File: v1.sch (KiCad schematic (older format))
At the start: 43 parts, among them J1 Conn_01x04, J101 K1X06, J102 FTDI, J103 ISP, J2 Conn_01x04, J3 Conn_01x04, J4 Conn_01x04, J5 Conn_01x04, Q1 AO3400A, SW101 SW_Push, U1 ATmega328P-AU, U3 PST61C24, U4 DS18B20, Y1 8MHz

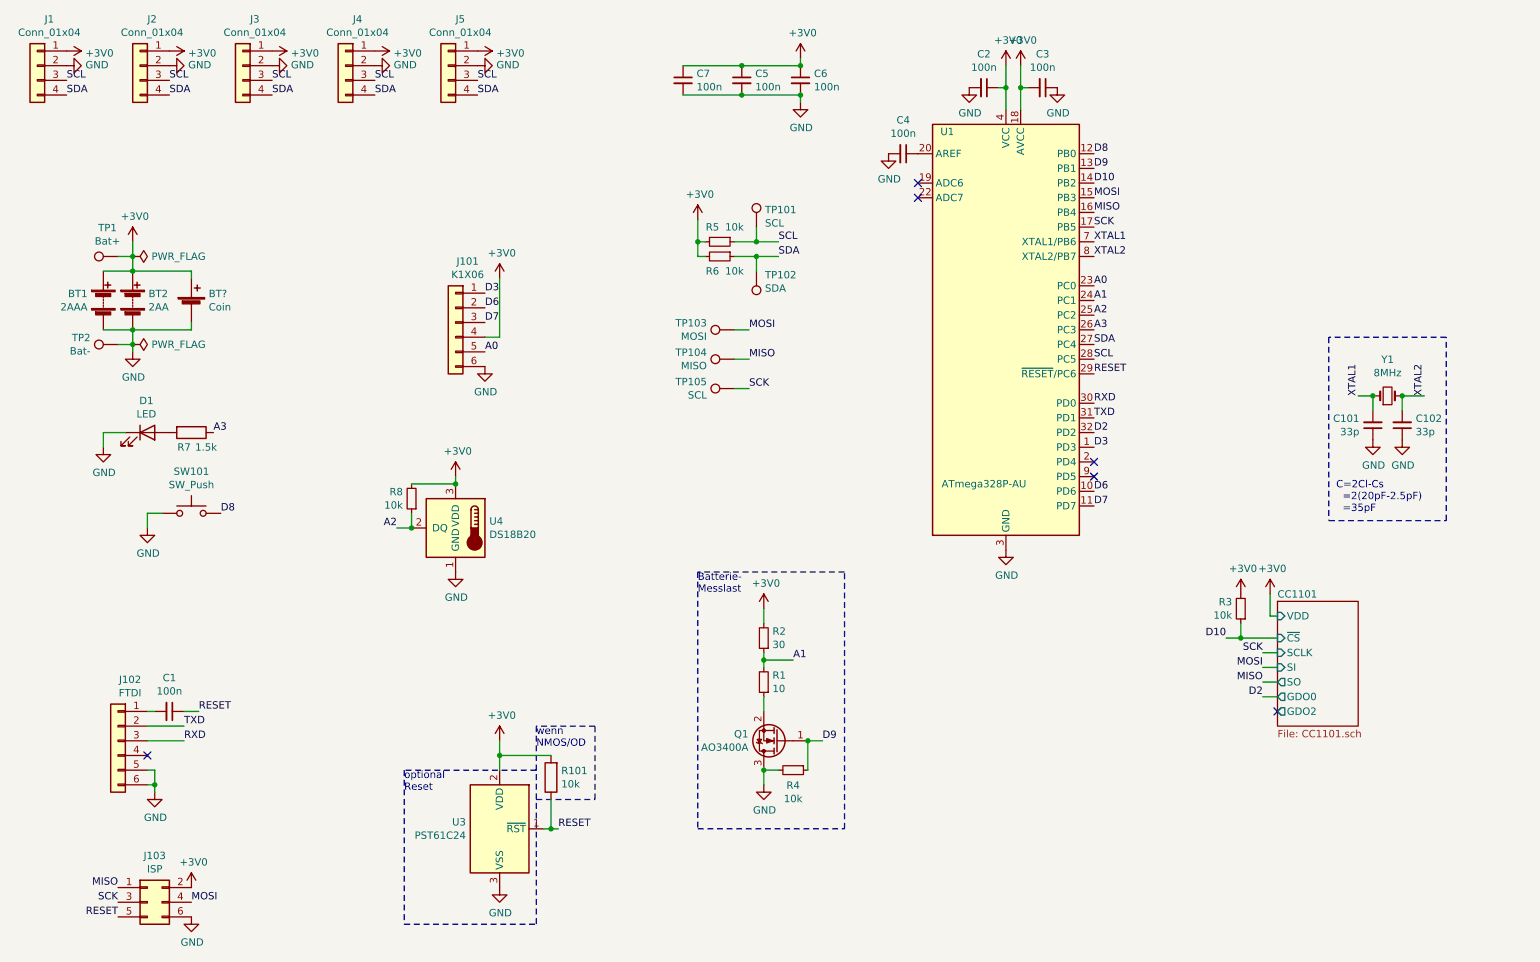
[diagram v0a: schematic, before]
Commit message: select more JLC components
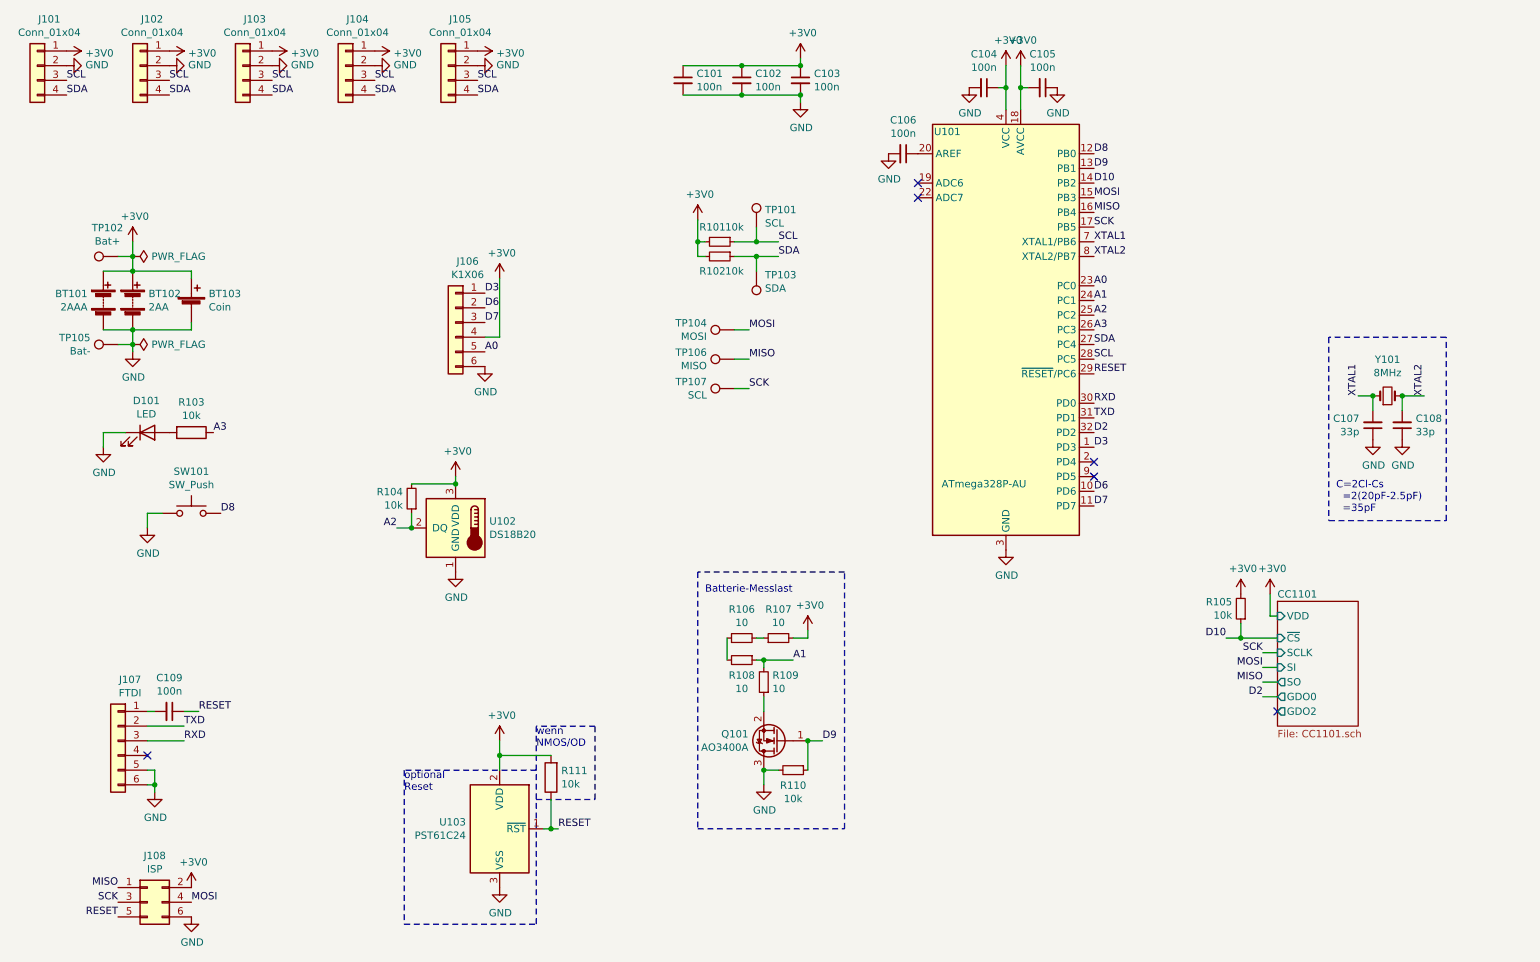
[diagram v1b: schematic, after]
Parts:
- removed R2: 30, Resistor_SMD:R_0402_1005Metric, symbol Device:R_Small
- added R106, R107, R108: 10, Resistor_SMD:R_0603_1608Metric, symbol Device:R_Small
- BT101: renamed from BT1; JLCPCB BOM (none) -> 0
- BT102: renamed from BT2; JLCPCB BOM (none) -> 0
- BT103: renamed from BT?; JLCPCB BOM (none) -> 0
- R103: renamed from R7; value 1.5k -> 10k; LCSC (none) -> C25804; Param (none) -> eigentlich 1.5k
- R109: renamed from R1; footprint Resistor_SMD:R_0402_1005Metric -> Resistor_SMD:R_0603_1608Metric; LCSC (none) -> C22859
- renumbered C7 to C101, C5 to C102, C6 to C103, C2 to C104, C3 to C105, C4 to C106, C101 to C107, C102 to C108, C1 to C109, D1 to D101, J1 to J101, J2 to J102, J3 to J103, J4 to J104, J5 to J105, J101 to J106, J102 to J107, J103 to J108, Q1 to Q101, R5 to R101, R6 to R102, R8 to R104, R3 to R105, R4 to R110, R101 to R111, TP1 to TP102, TP102 to TP103, TP103 to TP104, TP2 to TP105, TP104 to TP106, TP105 to TP107, U1 to U101, U4 to U102, U3 to U103, Y1 to Y101
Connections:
- net +3V0: now also R107.2
- net A1: now also R108.1
- new net: R106.1, R108.2
- new net: R106.2, R107.1
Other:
- note added: "Batterie-Messlast"
- note removed: "Batterie-\nMesslast"

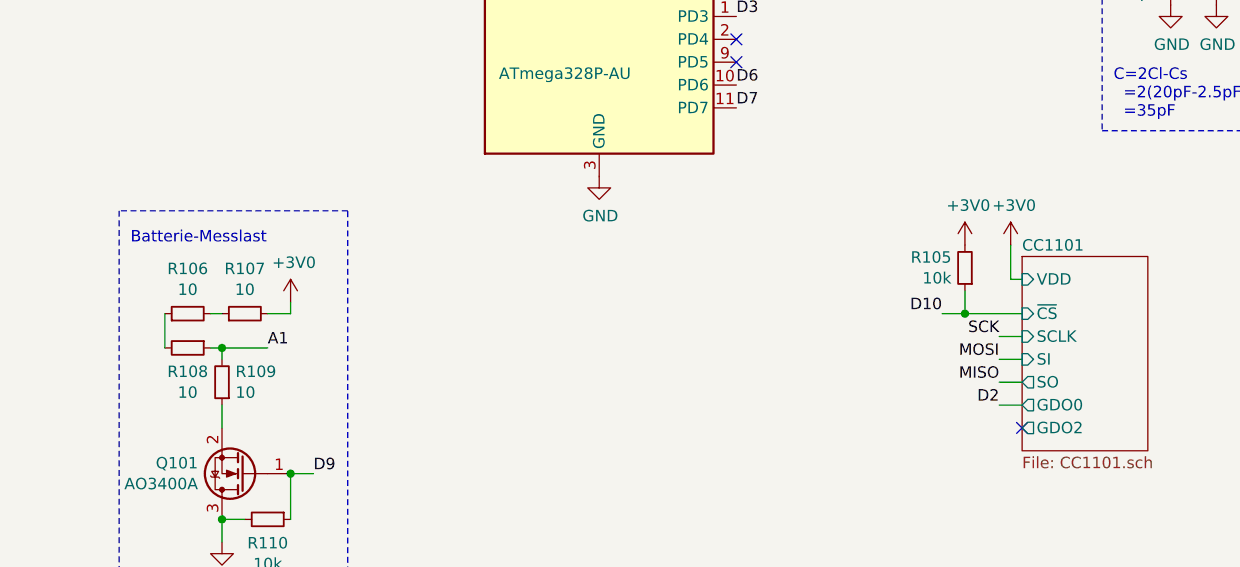
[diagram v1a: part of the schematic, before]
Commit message: raw component placement
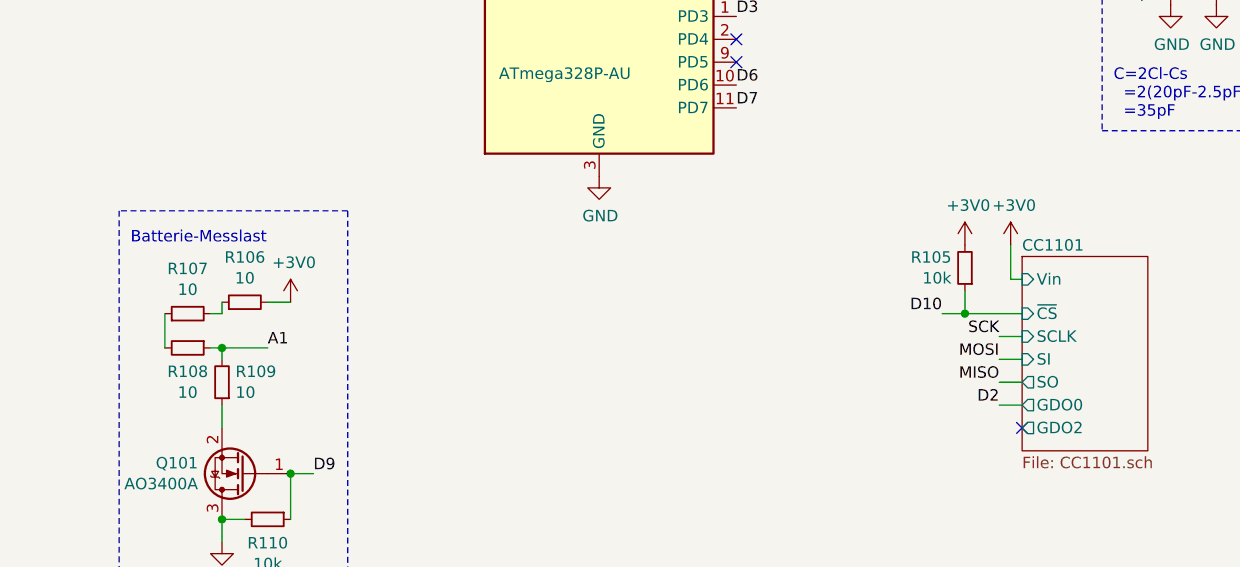
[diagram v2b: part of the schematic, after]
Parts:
- renumbered R107 to R106, R106 to R107
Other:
- moved on the sheet: R106
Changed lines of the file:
@@
 F6 "SI" I L 9150 5000 50
 F7 "GDO0" O L 9150 5200 50
-F8 "VDD" I L 9150 4650 50
+F8 "Vin" I L 9150 4650 50
 $EndSheet
 $Comp
@@
 	1150 2300 1350 2300
 $Comp
-L Device:R_Small R106
+L Device:R_Small R107
 U 1 1 608A12EC
 P 5500 4800
-F 0 "R106" V 5696 4800 50  0000 C CNN
+F 0 "R107" V 5696 4800 50  0000 C CNN
 F 1 "10" V 5605 4800 50  0000 C CNN
 F 2 "Resistor_SMD:R_0603_1608Metric" H 5500 4800 50  0001 C CNN
@@
 $EndComp
 $Comp
-L Device:R_Small R107
+L Device:R_Small R106
 U 1 1 608A182A
-P 5750 4800
-F 0 "R107" V 5946 4800 50  0000 C CNN
-F 1 "10" V 5855 4800 50  0000 C CNN
-F 2 "Resistor_SMD:R_0603_1608Metric" H 5750 4800 50  0001 C CNN
-F 3 "https://datasheet.lcsc.com/szlcsc/Uniroyal-Elec-0603WAF100JT5E_C22859.pdf" H 5750 4800 50  0001 C CNN
-F 4 "C22859" H 5750 4800 50  0001 C CNN "LCSC"
-	1    5750 4800
+P 5750 4750
+F 0 "R106" V 5946 4750 50  0000 C CNN
+F 1 "10" V 5855 4750 50  0000 C CNN
+F 2 "Resistor_SMD:R_0603_1608Metric" H 5750 4750 50  0001 C CNN
+F 3 "https://datasheet.lcsc.com/szlcsc/Uniroyal-Elec-0603WAF100JT5E_C22859.pdf" H 5750 4750 50  0001 C CNN
+F 4 "C22859" H 5750 4750 50  0001 C CNN "LCSC"
+	1    5750 4750
 	0    -1   -1   0
 $EndComp
@@
 	5400 4800 5400 4950
 Wire Wire Line
-	5850 4800 5950 4800
-Wire Wire Line
-	5950 4800 5950 4750
+	5850 4750 5950 4750
+Wire Wire Line
+	5650 4800 5650 4750
 $EndSCHEMATC

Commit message: place CC1101 circuits
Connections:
- net +3V0: no longer R105.2
- new net VDD: R105.2
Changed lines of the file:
@@
 	8900 4800 9150 4800
 $Comp
-L power:+3V0 #PWR0130
+L power:VDD #PWR0130
 U 1 1 608E504A
 P 8900 4500
 F 0 "#PWR0130" H 8900 4350 50  0001 C CNN
-F 1 "+3V0" H 8915 4673 50  0000 C CNN
+F 1 "VDD" H 8915 4673 50  0000 C CNN
 F 2 "" H 8900 4500 50  0001 C CNN
 F 3 "" H 8900 4500 50  0001 C CNN

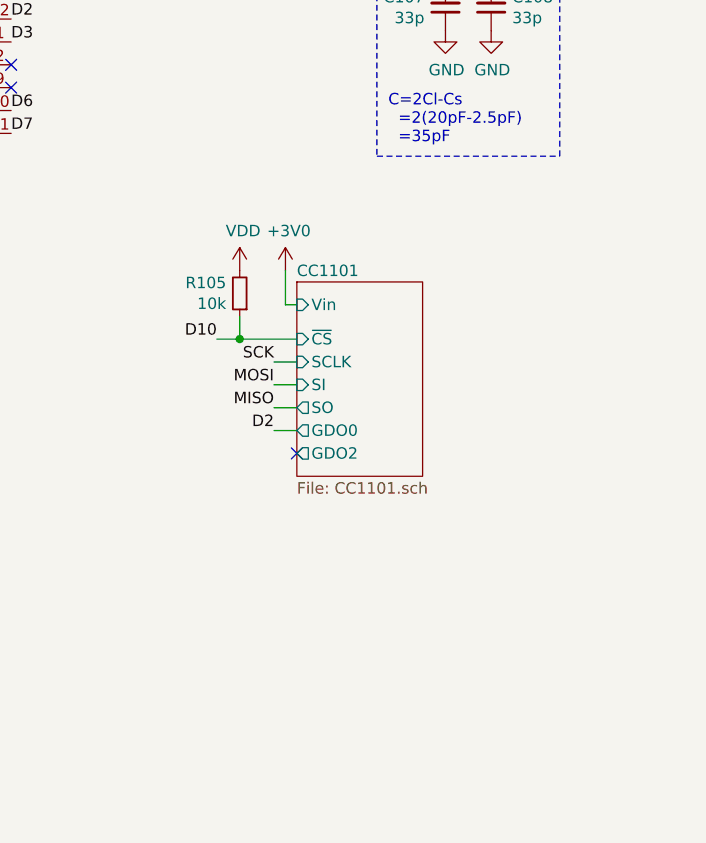
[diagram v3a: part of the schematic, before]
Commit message: adapt boards for kradex casings
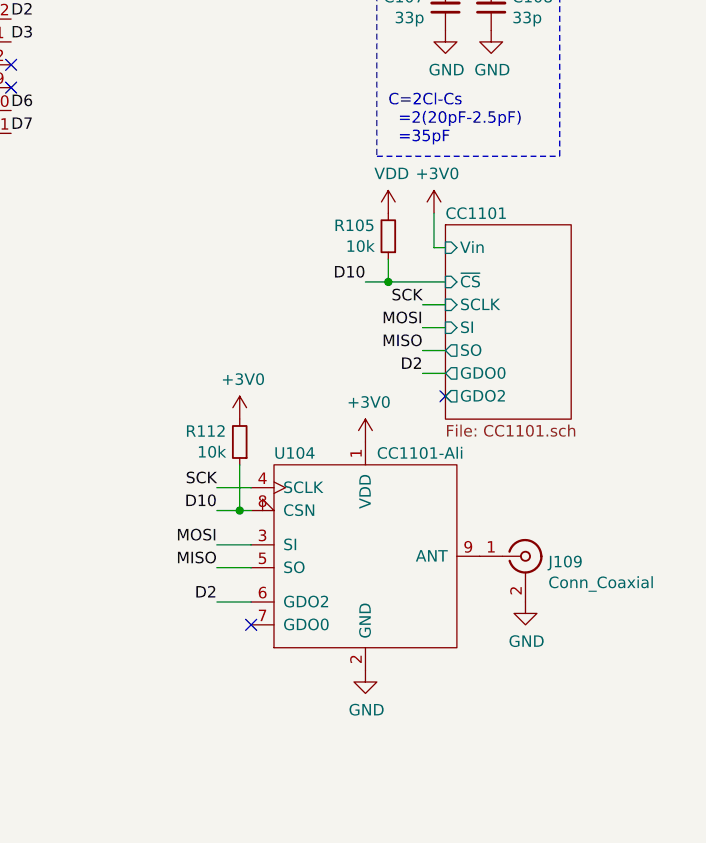
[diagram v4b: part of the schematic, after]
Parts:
- added J109: Conn_Coaxial, Connector_Coaxial:SMA_Amphenol_901-144_Vertical, symbol Connector:Conn_Coaxial
- added R112: 10k, Resistor_SMD:R_0402_1005Metric, symbol Device:R_Small
- added U104: CC1101-Ali, _project:CC1101-Ali, symbol _project:CC1101-Ali
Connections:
- net +3V0: now also R112.2, U104.1 (VDD)
- net D10: now also R112.1, U104.8 (CSN)
- net D2: now also U104.6 (GDO2)
- net GND: now also J109.2 (Ext), U104.2 (GND)
- net MISO: now also U104.5 (SO)
- net MOSI: now also U104.3 (SI)
- net SCK: now also U104.4 (SCLK)
- new net: J109.1 (In), U104.9 (ANT)
- no-connect marks 6 -> 7
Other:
- moved on the sheet: R105
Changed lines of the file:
@@
 L Device:R_Small R105
 U 1 1 6085DC9B
-P 8900 4600
-F 0 "R105" H 8959 4554 50  0000 L CNN
-F 1 "10k" H 8959 4645 50  0000 L CNN
-F 2 "Resistor_SMD:R_0402_1005Metric" H 8900 4600 50  0001 C CNN
-F 3 "https://datasheet.lcsc.com/szlcsc/Uniroyal-Elec-0603WAF1002T5E_C25804.pdf" H 8900 4600 50  0001 C CNN
-F 4 "C25804" H 8900 4600 50  0001 C CNN "LCSC"
-F 5 "Uniroyal 0603WAF1002T5E" H 8900 4600 50  0001 C CNN "Type"
-	1    8900 4600
+P 9550 4350
+F 0 "R105" H 9609 4304 50  0000 L CNN
+F 1 "10k" H 9609 4395 50  0000 L CNN
+F 2 "Resistor_SMD:R_0402_1005Metric" H 9550 4350 50  0001 C CNN
+F 3 "https://datasheet.lcsc.com/szlcsc/Uniroyal-Elec-0603WAF1002T5E_C25804.pdf" H 9550 4350 50  0001 C CNN
+F 4 "C25804" H 9550 4350 50  0001 C CNN "LCSC"
+F 5 "Uniroyal 0603WAF1002T5E" H 9550 4350 50  0001 C CNN "Type"
+	1    9550 4350
 	-1   0    0    1
 $EndComp
@@
 optional\nReset
 $Sheet
-S 9150 4550 550  850
+S 9800 4300 550  850
 U 6084C09B
 F0 "CC1101" 50
 F1 "CC1101.sch" 50
-F2 "SO" O L 9150 5100 50
-F3 "GDO2" O L 9150 5300 50
-F4 "~CS" I L 9150 4800 50
-F5 "SCLK" I L 9150 4900 50
-F6 "SI" I L 9150 5000 50
-F7 "GDO0" O L 9150 5200 50
-F8 "Vin" I L 9150 4650 50
+F2 "SO" O L 9800 4850 50
+F3 "GDO2" O L 9800 5050 50
+F4 "~CS" I L 9800 4550 50
+F5 "SCLK" I L 9800 4650 50
+F6 "SI" I L 9800 4750 50
+F7 "GDO0" O L 9800 4950 50
+F8 "Vin" I L 9800 4400 50
 $EndSheet
 $Comp
 L power:+3V0 #PWR0131
 U 1 1 608D11F6
-P 9100 4500
-F 0 "#PWR0131" H 9100 4350 50  0001 C CNN
-F 1 "+3V0" H 9115 4673 50  0000 C CNN
-F 2 "" H 9100 4500 50  0001 C CNN
-F 3 "" H 9100 4500 50  0001 C CNN
-	1    9100 4500
-	1    0    0    -1
-$EndComp
-Wire Wire Line
-	9150 4650 9100 4650
-Wire Wire Line
-	9100 4650 9100 4500
-Text Label 8800 4800 2    50   ~ 0
+P 9750 4250
+F 0 "#PWR0131" H 9750 4100 50  0001 C CNN
+F 1 "+3V0" H 9765 4423 50  0000 C CNN
+F 2 "" H 9750 4250 50  0001 C CNN
+F 3 "" H 9750 4250 50  0001 C CNN
+	1    9750 4250
+	1    0    0    -1
+$EndComp
+Wire Wire Line
+	9800 4400 9750 4400
+Wire Wire Line
+	9750 4400 9750 4250
+Text Label 9450 4550 2    50   ~ 0
 D10
-Text Label 9050 4900 2    50   ~ 0
+Text Label 9700 4650 2    50   ~ 0
 SCK
-Text Label 9050 5000 2    50   ~ 0
+Text Label 9700 4750 2    50   ~ 0
 MOSI
-Text Label 9050 5100 2    50   ~ 0
+Text Label 9700 4850 2    50   ~ 0
 MISO
-Text Label 9050 5200 2    50   ~ 0
+Text Label 9700 4950 2    50   ~ 0
 D2
 Wire Wire Line
-	9050 4900 9150 4900
-Wire Wire Line
-	9150 5000 9050 5000
-Wire Wire Line
-	9050 5100 9150 5100
-Wire Wire Line
-	9150 5200 9050 5200
-NoConn ~ 9150 5300
-Wire Wire Line
-	8800 4800 8900 4800
-Wire Wire Line
-	8900 4800 8900 4700
-Connection ~ 8900 4800
-Wire Wire Line
-	8900 4800 9150 4800
+	9700 4650 9800 4650
+Wire Wire Line
+	9800 4750 9700 4750
+Wire Wire Line
+	9700 4850 9800 4850
+Wire Wire Line
+	9800 4950 9700 4950
+NoConn ~ 9800 5050
+Wire Wire Line
+	9450 4550 9550 4550
+Wire Wire Line
+	9550 4550 9550 4450
+Connection ~ 9550 4550
+Wire Wire Line
+	9550 4550 9800 4550
 $Comp
 L power:VDD #PWR0130
 U 1 1 608E504A
-P 8900 4500
-F 0 "#PWR0130" H 8900 4350 50  0001 C CNN
-F 1 "VDD" H 8915 4673 50  0000 C CNN
-F 2 "" H 8900 4500 50  0001 C CNN
-F 3 "" H 8900 4500 50  0001 C CNN
-	1    8900 4500
+P 9550 4250
+F 0 "#PWR0130" H 9550 4100 50  0001 C CNN
+F 1 "VDD" H 9565 4423 50  0000 C CNN
+F 2 "" H 9550 4250 50  0001 C CNN
+F 3 "" H 9550 4250 50  0001 C CNN
+	1    9550 4250
 	1    0    0    -1
 $EndComp
@@
 Wire Wire Line
 	5650 4800 5650 4750
+$Comp
+L _project:CC1101-Ali U104
+U 1 1 6090B1D0
+P 9450 5750
+F 0 "U104" H 9050 6200 50  0000 L CNN
+F 1 "CC1101-Ali" H 9500 6200 50  0000 L CNN
+F 2 "_project:CC1101-Ali" H 10000 5250 50  0001 C CNN
+F 3 "https://www.aliexpress.com/item/32472259186.html?spm=a2g0o.productlist.0.0.16eb1ce1Gheynz&algo_pvid=48bd72b3-87b0-4c3d-8a67-cc00581764a7&algo_expid=48bd72b3-87b0-4c3d-8a67-cc00581764a7-42&btsid=2100bdf016200726669482167e3db0&ws_ab_test=searchweb0_0,searchweb201602_,searchweb201603_" H 9500 5700 50  0001 C CNN
+	1    9450 5750
+	1    0    0    -1
+$EndComp
+$Comp
+L power:GND #PWR0141
+U 1 1 6090BAF3
+P 9450 6250
+F 0 "#PWR0141" H 9450 6000 50  0001 C CNN
+F 1 "GND" H 9455 6077 50  0000 C CNN
+F 2 "" H 9450 6250 50  0001 C CNN
+F 3 "" H 9450 6250 50  0001 C CNN
+	1    9450 6250
+	1    0    0    -1
+$EndComp
+$Comp
+L Device:R_Small R112
+U 1 1 6090BD9D
+P 8900 5250
+F 0 "R112" H 8959 5204 50  0000 L CNN
+F 1 "10k" H 8959 5295 50  0000 L CNN
+F 2 "Resistor_SMD:R_0402_1005Metric" H 8900 5250 50  0001 C CNN
+F 3 "https://datasheet.lcsc.com/szlcsc/Uniroyal-Elec-0603WAF1002T5E_C25804.pdf" H 8900 5250 50  0001 C CNN
+F 4 "C25804" H 8900 5250 50  0001 C CNN "LCSC"
+F 5 "Uniroyal 0603WAF1002T5E" H 8900 5250 50  0001 C CNN "Type"
+	1    8900 5250
+	-1   0    0    1
+$EndComp
+$Comp
+L power:+3V0 #PWR0139
+U 1 1 6090CB5B
+P 8900 5150
+F 0 "#PWR0139" H 8900 5000 50  0001 C CNN
+F 1 "+3V0" H 8915 5323 50  0000 C CNN
+F 2 "" H 8900 5150 50  0001 C CNN
+F 3 "" H 8900 5150 50  0001 C CNN
+	1    8900 5150
+	1    0    0    -1
+$EndComp
+$Comp
+L power:+3V0 #PWR0140
+U 1 1 6090CDB3
+P 9450 5250
+F 0 "#PWR0140" H 9450 5100 50  0001 C CNN
+F 1 "+3V0" H 9465 5423 50  0000 C CNN
+F 2 "" H 9450 5250 50  0001 C CNN
+F 3 "" H 9450 5250 50  0001 C CNN
+	1    9450 5250
+	1    0    0    -1
+$EndComp
+Text Label 8800 5450 2    50   ~ 0
+SCK
+Wire Wire Line
+	8800 5450 8950 5450
+Text Label 8800 5700 2    50   ~ 0
+MOSI
+Text Label 8800 5800 2    50   ~ 0
+MISO
+Text Label 8800 5950 2    50   ~ 0
+D2
+Text Label 8800 5550 2    50   ~ 0
+D10
+Wire Wire Line
+	8950 5550 8900 5550
+Wire Wire Line
+	8800 5700 8950 5700
+Wire Wire Line
+	8950 5800 8800 5800
+Wire Wire Line
+	8800 5950 8950 5950
+Wire Wire Line
+	8900 5350 8900 5550
+Connection ~ 8900 5550
+Wire Wire Line
+	8900 5550 8800 5550
+NoConn ~ 8950 6050
+$Comp
+L Connector:Conn_Coaxial J109
+U 1 1 60938A79
+P 10150 5750
+F 0 "J109" H 10250 5725 50  0000 L CNN
+F 1 "Conn_Coaxial" H 10250 5634 50  0000 L CNN
+F 2 "Connector_Coaxial:SMA_Amphenol_901-144_Vertical" H 10150 5750 50  0001 C CNN
+F 3 " ~" H 10150 5750 50  0001 C CNN
+	1    10150 5750
+	1    0    0    -1
+$EndComp
+$Comp
+L power:GND #PWR0142
+U 1 1 609391C9
+P 10150 5950
+F 0 "#PWR0142" H 10150 5700 50  0001 C CNN
+F 1 "GND" H 10155 5777 50  0000 C CNN
+F 2 "" H 10150 5950 50  0001 C CNN
+F 3 "" H 10150 5950 50  0001 C CNN
+	1    10150 5950
+	1    0    0    -1
+$EndComp
 $EndSCHEMATC
